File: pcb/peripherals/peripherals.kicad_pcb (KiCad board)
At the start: 2 copper layers, 113.5 x 124.5 mm, 122 parts, among them J101 Conn_01x05, J102 Conn_01x05, J103 Conn_01x04, J104 Conn_01x04, J105 Conn_01x04, J106 Conn_01x04, J107 Conn_01x05, J108 Conn_01x05, Q201 RQ3E100BNTB, Q202 RQ3E100BNTB, Q301 RQ3E100BNTB, Q302 RQ3E100BNTB, Q401 RQ3E100BNTB, Q402 RQ3E100BNTB, Q501 RQ3E100BNTB, Q502 RQ3E100BNTB, Q601 RQ3E100BNTB, Q602 RQ3E100BNTB, Q701 RQ3E100BNTB, Q702 RQ3E100BNTB, Q801 RQ3E100BNTB, Q802 RQ3E100BNTB, Q901 RQ3E100BNTB, Q902 RQ3E100BNTB, U201 DGD0506A, U301 DGD0506A, U401 DGD0506A, U501 DGD0506A, U601 DGD0506A, U701 DGD0506A, U801 DGD0506A, U901 DGD0506A

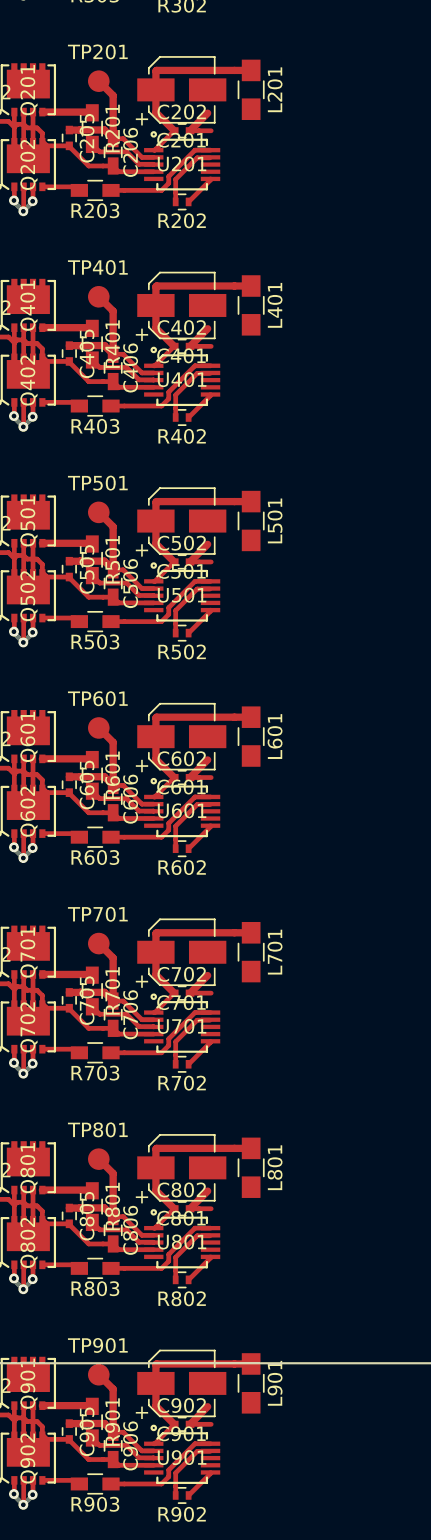
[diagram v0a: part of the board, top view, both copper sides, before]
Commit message: Autotile again, with copying of global traces/vias enabled
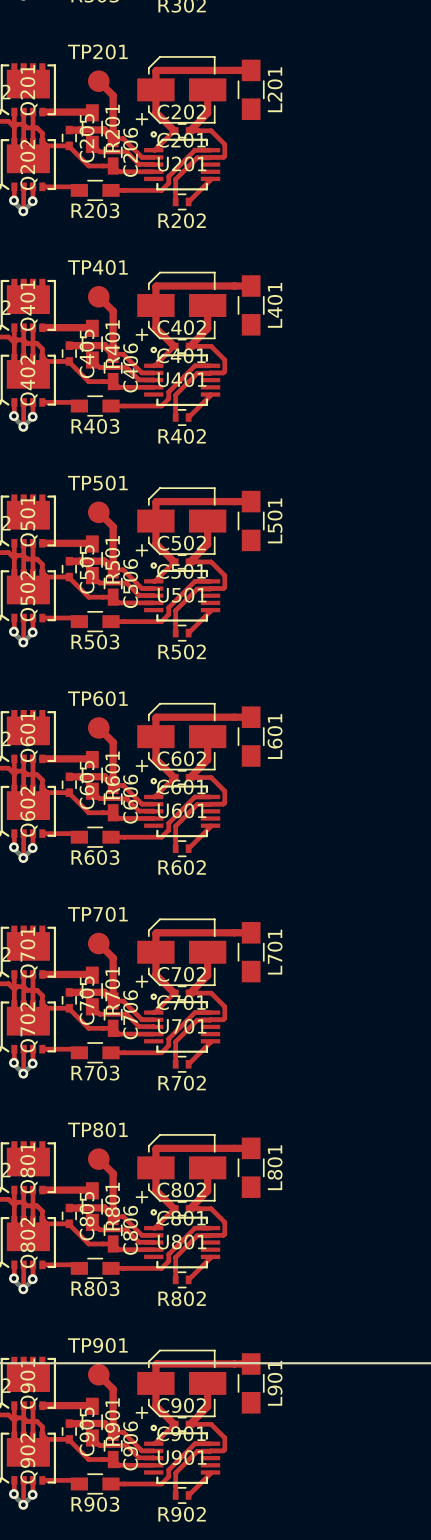
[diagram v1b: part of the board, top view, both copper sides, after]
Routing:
- net GND: track 112.5 -> 146.4 mm

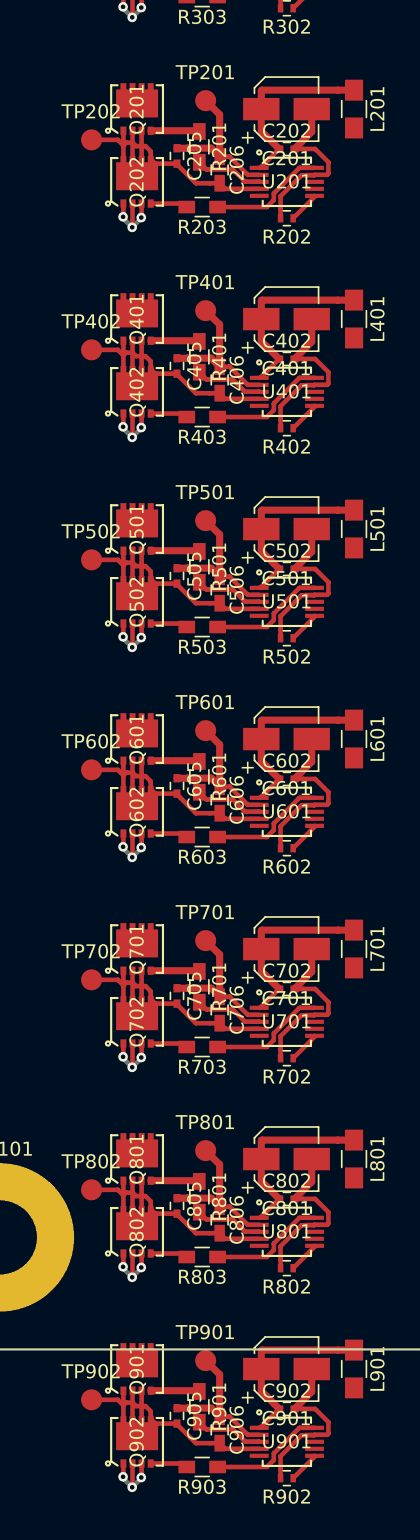
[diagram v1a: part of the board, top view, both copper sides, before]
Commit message: Disable the thing I just did because it wasn't correct
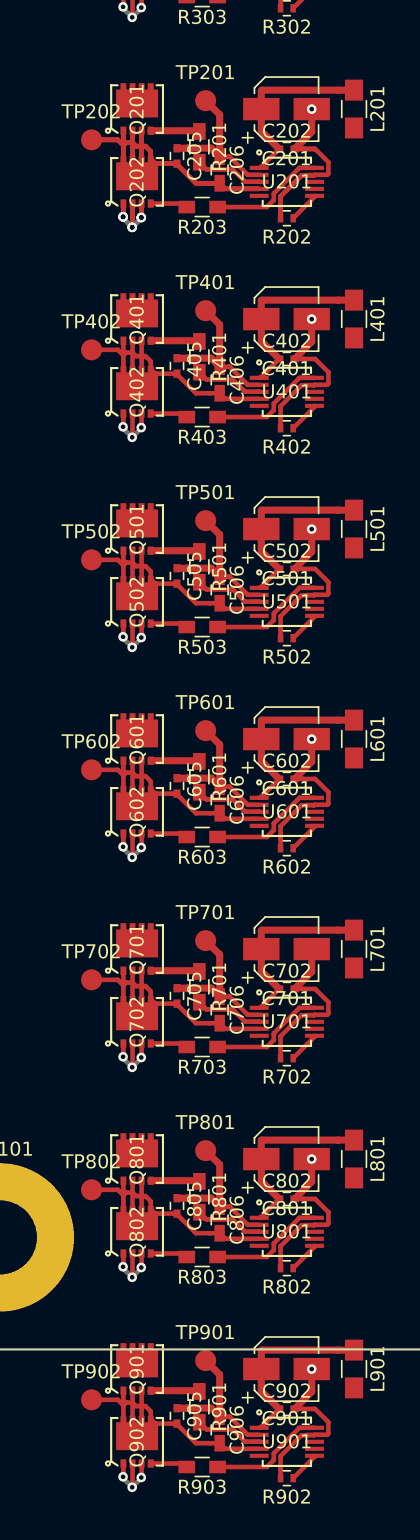
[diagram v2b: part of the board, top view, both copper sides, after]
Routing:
- net /sheet5B6E69B5/OUT: track 173.2 -> 21.6 mm
- net /Sheet5B7230C3/OUT: track 0.00 -> 43.3 mm
- net /sheet5B6E6A5D/OUT: track 0.00 -> 21.6 mm
- net /sheet5B6E6A5C/OUT: track 0.00 -> 21.6 mm
- net /sheet5B6E6A5B/OUT: track 0.00 -> 21.6 mm
- net /sheet5B6E6A5A/OUT: track 0.00 -> 21.6 mm
- net /sheet5B6E69C4/OUT: track 0.00 -> 21.6 mm
- net /sheet5B6E69C3/OUT: track 0.00 -> 21.6 mm
- net GND: track 146.4 -> 159.9 mm, vias 25 -> 34
- net +BATT: track 47.8 -> 53.8 mm

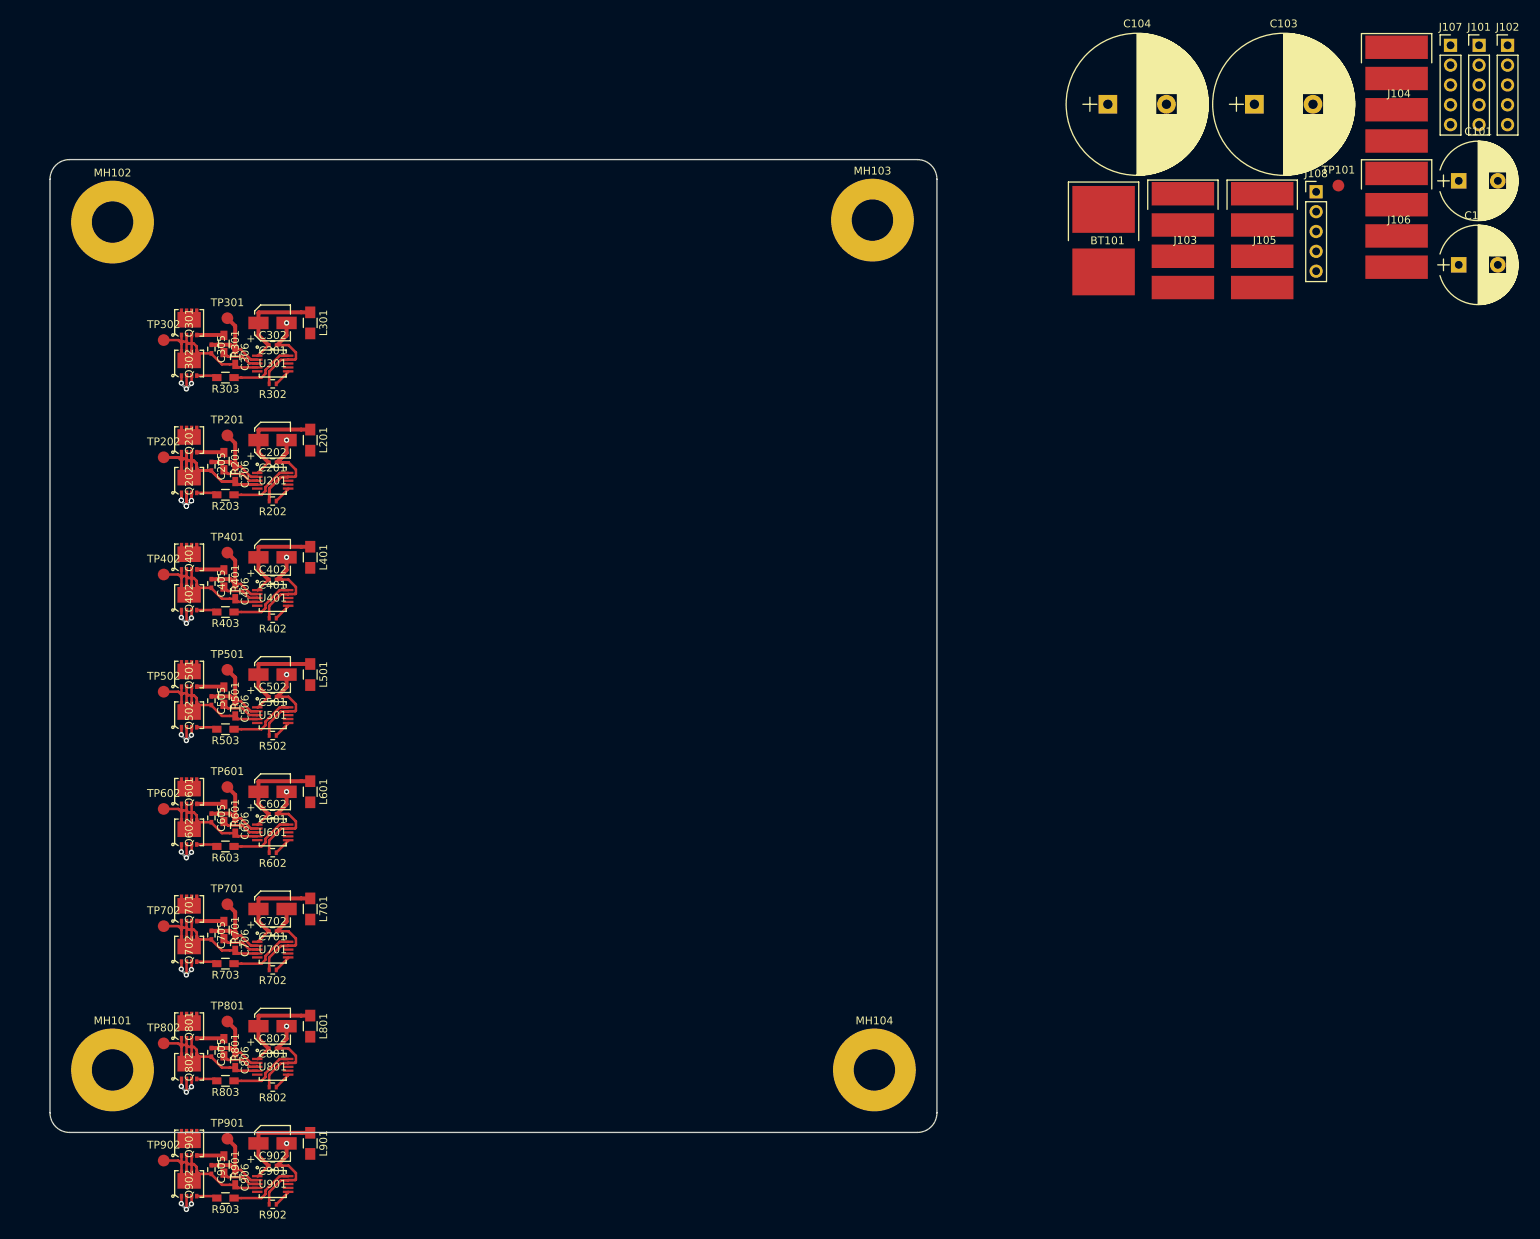
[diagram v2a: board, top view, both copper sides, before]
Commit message: Redesign peripheral PCB, simulate photodiode circuit
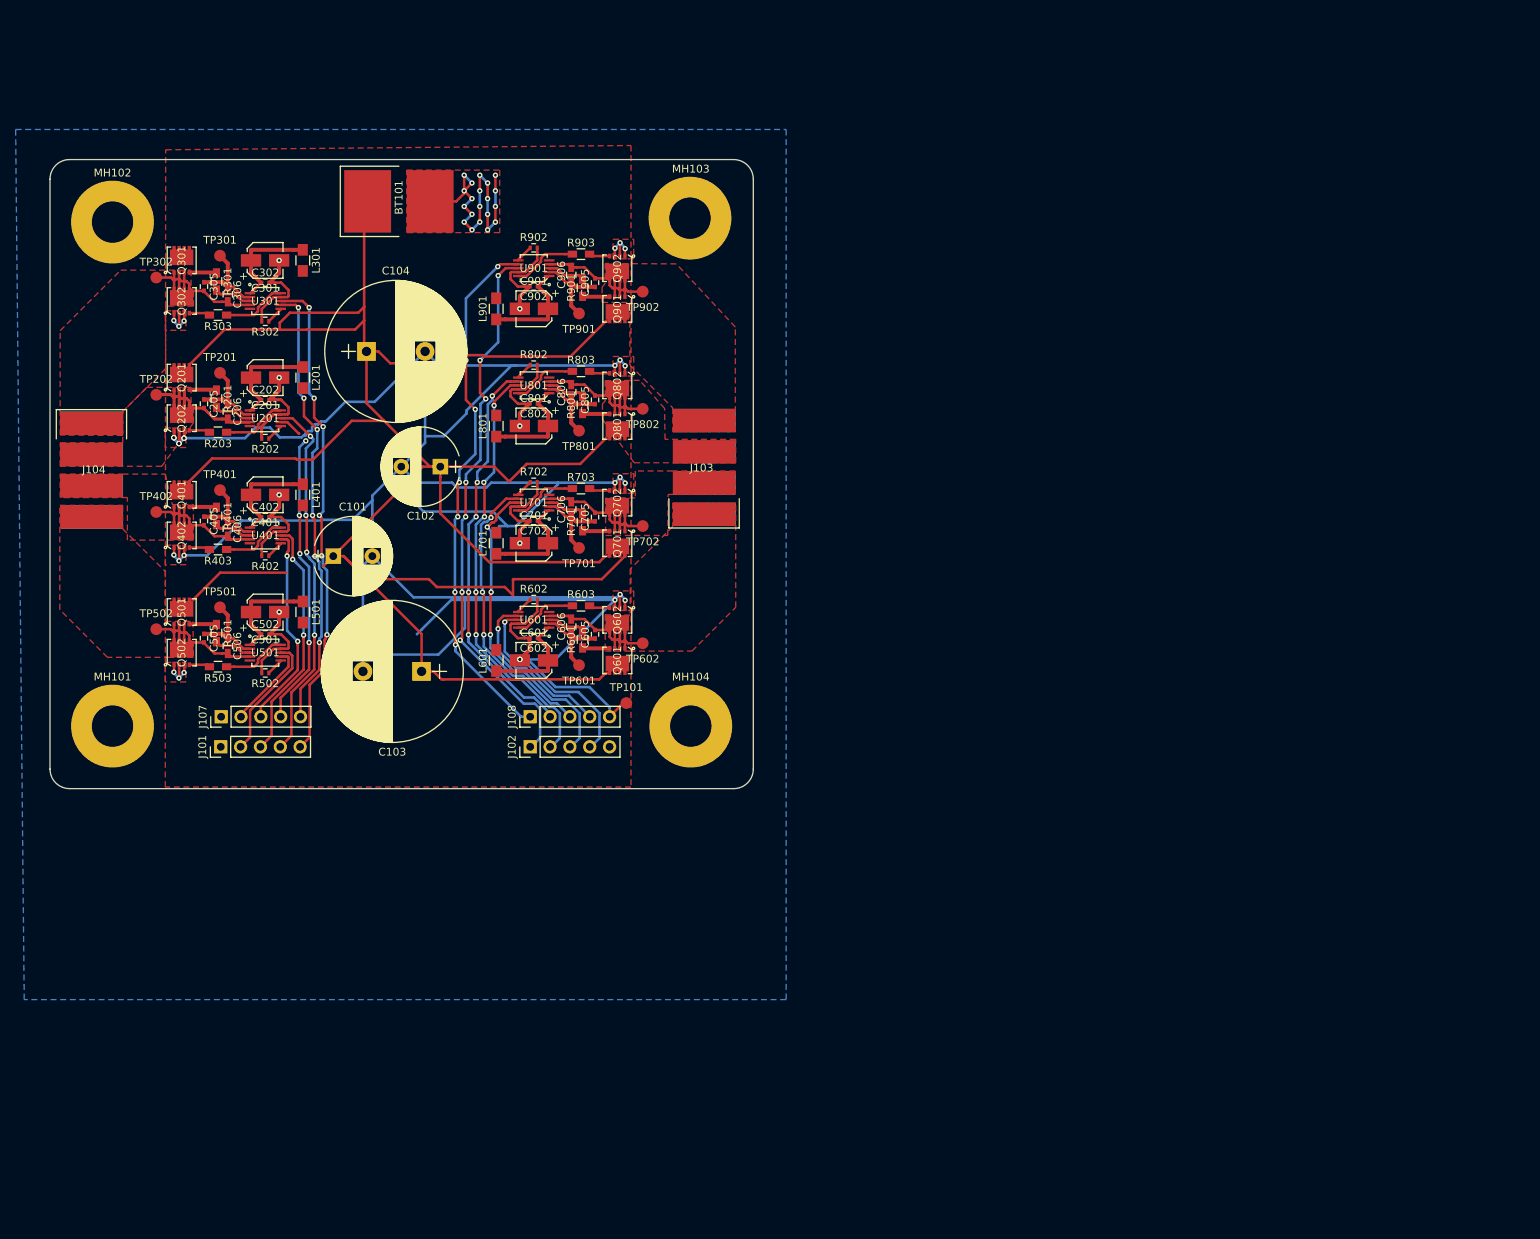
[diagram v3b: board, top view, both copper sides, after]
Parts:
- J105, J106: moved to B.Cu
- R202, R302, R402, R502, R602, R702, R802, R902: value 10k -> 100k
- moved J101 184.4 mm to (55.9, 122.7), turned to 90 degrees
- moved J107 179.3 mm to (55.9, 118.8), turned to 90 degrees
- moved J104 173.8 mm to (39.3, 87.2)
- moved J102 154.0 mm to (95.5, 122.7), turned to 90 degrees
- moved J105 152.6 mm to (39.4, 87.2)
- moved C101 151.8 mm to (70.2, 98.2)
- moved C102 132.9 mm to (84.0, 86.8), turned to 180 degrees
- moved Q902 129.4 mm to (106.6, 61.4), turned to 270 degrees
- moved R903 129.1 mm to (102.0, 59.6), turned to 0 degrees
- moved C103 128.9 mm to (81.5, 113.0), turned to 180 degrees
- moved TP902 127.0 mm to (109.8, 64.4), turned to 180 degrees
- moved R902 126.9 mm to (95.9, 58.8), turned to 0 degrees
- moved C905 123.7 mm to (103.8, 63.2), turned to 90 degrees
- moved C906 123.2 mm to (100.7, 62.2), turned to 90 degrees
- moved U901 121.9 mm to (95.9, 61.4), turned to 180 degrees
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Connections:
- J101 pad 4: /sheet5B6E69B5/IN -> /Sheet5B7230C3/IN
- J101 pad 5: /Sheet5B7230C3/IN -> /sheet5B6E69B5/IN
- J102 pad 1: GND -> /sheet5B6E6A5D/IN
- J102 pad 2: /sheet5B6E6A5D/IN -> /sheet5B6E6A5C/IN
- J102 pad 3: /sheet5B6E6A5C/IN -> /sheet5B6E6A5B/IN
- J102 pad 4: /sheet5B6E6A5B/IN -> /sheet5B6E6A5A/IN
- J102 pad 5: /sheet5B6E6A5A/IN -> GND
- J104 pad 1: /Sheet5B7230C3/OUT -> /sheet5B6E69B5/OUT
- J104 pad 2: /sheet5B6E69B5/OUT -> /Sheet5B7230C3/OUT
- J107 pad 4: /sheet5B6E69B5/EN -> /Sheet5B7230C3/EN
- J107 pad 5: /Sheet5B7230C3/EN -> /sheet5B6E69B5/EN
- J108 pad 1: GND -> /sheet5B6E6A5D/EN
- J108 pad 2: /sheet5B6E6A5D/EN -> /sheet5B6E6A5C/EN
- J108 pad 3: /sheet5B6E6A5C/EN -> /sheet5B6E6A5B/EN
- J108 pad 4: /sheet5B6E6A5B/EN -> /sheet5B6E6A5A/EN
- J108 pad 5: /sheet5B6E6A5A/EN -> GND
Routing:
- net GND: track 159.9 -> 513.8 mm, vias 34 -> 56
- net +BATT: track 53.8 -> 366.0 mm
- net /sheet5B6E6A5D/IN: track 0.00 -> 71.5 mm, vias 0 -> 7
- net /sheet5B6E6A5D/EN: track 0.00 -> 68.3 mm, vias 0 -> 7
- net /sheet5B6E69B5/IN: track 0.00 -> 63.0 mm, vias 0 -> 6
- net /sheet5B6E69B5/EN: track 0.00 -> 57.6 mm, vias 0 -> 6
- net /sheet5B6E6A5C/IN: track 0.00 -> 55.3 mm, vias 0 -> 5
- net /sheet5B6E6A5C/EN: track 0.00 -> 51.6 mm, vias 0 -> 5
- net /Sheet5B7230C3/IN: track 0.00 -> 47.4 mm, vias 0 -> 4
- net /sheet5B6E6A5B/IN: track 0.00 -> 41.0 mm, vias 0 -> 3
- net /Sheet5B7230C3/EN: track 0.00 -> 40.8 mm, vias 0 -> 4
- net /sheet5B6E6A5B/EN: track 0.00 -> 37.0 mm, vias 0 -> 3
- net /sheet5B6E69C3/IN: track 0.00 -> 31.2 mm, vias 0 -> 2
- net /sheet5B6E69C3/EN: track 0.00 -> 26.2 mm, vias 0 -> 2
- net /sheet5B6E6A5A/IN: track 0.00 -> 25.9 mm, vias 0 -> 1
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- added copper zone on F.Cu, net +BATT
- added copper zone on F.Cu, net /Sheet5B7230C3/OUT
- added copper zone on F.Cu, net /sheet5B6E69B5/OUT
- added copper zone on F.Cu, net /sheet5B6E69C3/OUT
- added copper zone on F.Cu, net /sheet5B6E69C4/OUT
- added copper zone on F.Cu, net /sheet5B6E6A5A/OUT
- added copper zone on F.Cu, net /sheet5B6E6A5B/OUT
- added copper zone on F.Cu, net /sheet5B6E6A5C/OUT
- added copper zone on F.Cu, net /sheet5B6E6A5D/OUT
- added copper zone on B.Cu, net GND
- added copper zone on F.Cu, net GND
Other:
- board size 113.5 x 124.5 mm -> 90 x 80.5 mm

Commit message: Regenerate Gerbers
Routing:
- net /Sheet5B7230C3/EN: track 40.8 -> 42.1 mm
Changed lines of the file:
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@@
     (thickness 1.6)
     (drawings 9)
-    (tracks 1348)
+    (tracks 1350)
     (zones 0)
     (modules 122)
@@
   )
   (setup
-    (last_trace_width 0.1524)
+    (last_trace_width 0.3302)
     (user_trace_width 0.1524)
     (user_trace_width 0.2032)
@@
   (gr_line (start 124 50) (end 124 125.5) (layer Edge.Cuts) (width 0.1524))
   (gr_line (start 36.5 47.5) (end 121.5 47.5) (layer Edge.Cuts) (width 0.1524))
-  (gr_text "FABRICATION NOTES\n\n1. THIS IS A 2 LAYER BOARD. \n2. EXTERNAL LAYERS SHALL HAVE 1 OZ COPPER.\n3. MATERIAL: FR4 AND 0.062 INCH +/- 10% THICK.\n4. BOARDS SHALL BE ROHS COMPLIANT. \n5. MANUFACTURE IN ACCORDANCE WITH IPC-6012 CLASS 2\n6. MASK: BOTH SIDES OF THE BOARD SHALL HAVE \n   SOLDER MASK (ANY COLOR) OVER BARE COPPER. \n7. SILK: BOTH SIDES OF THE BOARD SHALL HAVE \n   WHITE SILKSCREEN. DO NOT PLACE SILK OVER BARE COPPER.\n8. FINISH: ENIG.\n9. MINIMUM TRACE WIDTH - 0.006 INCH.\n   MINIMUM SPACE - 0.006 INCH.\n   MINIMUM HOLE DIA - 0.013 INCH. \n10. MAX HOLE PLACEMENT TOLERANCE OF +/- 0.003 INCH.\n11. MAX HOLE DIAMETER TOLERANCE OF +/- 0.003 INCH AFTER PLATING." (at 153.75 127.4) (layer Dwgs.User)
+  (gr_text "FABRICATION NOTES\n\n1. THIS IS A 2 LAYER BOARD. \n2. EXTERNAL LAYERS SHALL HAVE 1 OZ COPPER.\n3. MATERIAL: FR4 AND 0.062 INCH +/- 10% THICK.\n4. BOARDS SHALL BE ROHS COMPLIANT. \n5. MANUFACTURE IN ACCORDANCE WITH IPC-6012 CLASS 2\n6. MASK: BOTH SIDES OF THE BOARD SHALL HAVE \n   SOLDER MASK (ANY COLOR) OVER BARE COPPER. \n7. SILK: BOTH SIDES OF THE BOARD SHALL HAVE \n   WHITE SILKSCREEN. DO NOT PLACE SILK OVER BARE COPPER.\n8. FINISH: HASL/ENIG.\n9. MINIMUM TRACE WIDTH - 0.006 INCH.\n   MINIMUM SPACE - 0.006 INCH.\n   MINIMUM HOLE DIA - 0.013 INCH. \n10. MAX HOLE PLACEMENT TOLERANCE OF +/- 0.003 INCH.\n11. MAX HOLE DIAMETER TOLERANCE OF +/- 0.003 INCH AFTER PLATING." (at 153.75 127.4) (layer Dwgs.User)
     (effects (font (size 2.54 2.54) (thickness 0.254)) (justify left))
   )
@@
   (segment (start 65.911787 93.03959) (end 65.911787 84.322174) (width 0.3302) (layer B.Cu) (net 80))
   (via (at 66.735125 83.498836) (size 0.6858) (drill 0.3302) (layers F.Cu B.Cu) (net 80))
+  (segment (start 65.845982 82.609693) (end 66.735125 83.498836) (width 0.3302) (layer F.Cu) (net 80))
+  (segment (start 65.845982 82.578497) (end 65.845982 82.609693) (width 0.3302) (layer F.Cu) (net 80))
   (via (at 67.85 108.35) (size 0.6858) (drill 0.3302) (layers F.Cu B.Cu) (net 81))
   (segment (start 67.85 108.834933) (end 67.85 108.35) (width 0.3302) (layer F.Cu) (net 81))
